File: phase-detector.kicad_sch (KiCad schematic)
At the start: 32 parts, among them J1 Conn_Coaxial_Small, J2 Conn_Coaxial_Small, J3 Conn_Coaxial_Small, J4 Conn_Coaxial_Small, J5 Conn_Coaxial_Small, J6 Conn_Coaxial_Small, J7 Conn_01x14_Socket, U1 ICM-20948, U2 MIC5219-3.3YM5, U3 MIC5219-3.3YM5

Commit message: Rev 1 ready for review
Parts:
- removed U1: ICM-20948, Sensor_Motion:InvenSense_QFN-24_3x3mm_P0.4mm, symbol Sensor_Motion:ICM-20948
- added TP1: INT_2, phase-detector:Test_Via, symbol Connector:TestPoint
- added TP10, TP11, TP12, TP13, TP9: ~{IRQ}, phase-detector:Test_Via, symbol Connector:TestPoint
- added TP2: DRDY, phase-detector:Test_Via, symbol Connector:TestPoint
- added TP3: INT_1, phase-detector:Test_Via, symbol Connector:TestPoint
- added TP4, TP5, TP6, TP7, TP8: Vref, phase-detector:Test_Via, symbol Connector:TestPoint
- added U14: LSM303C, Package_LGA:LGA-12_2x2mm_P0.5mm, symbol Sensor_Motion:LSM303C
- C1: footprint (none) -> Capacitor_SMD:C_0402_1005Metric
- C136, C137, C138, C139: value 10nF -> 100pF
- C2: footprint (none) -> Capacitor_SMD:C_0805_2012Metric
- C5: value 100nF -> 220nF
- R43, R44, R45, R46: value 50 -> 75
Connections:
- net +3.3V-D: now also U14.10 (VDDIO), U14.9 (VDD)
- net AD8302/V_REF: now also TP4.1
- net AD8303/V_REF: now also TP5.1
- net AD8304/V_REF: now also TP6.1
- net AD8305/V_REF: now also TP7.1
- net AD8306/V_REF: now also TP8.1
- net ADC/MDAT: now also TP9.1
- net ADC1/MDAT: now also TP10.1
- net ADC2/MDAT: now also TP11.1
- net ADC3/MDAT: now also TP12.1
- net ADC4/MDAT: now also TP13.1
- net CS0: now also J7.8 (Pin_8); no longer J7.7 (Pin_7)
- net CS1: now also J7.11 (Pin_11); no longer J7.8 (Pin_8)
- net CS2: now also J7.12 (Pin_12); no longer J7.9 (Pin_9)
- net CS3: now also J7.9 (Pin_9); no longer J7.10 (Pin_10)
- net CS4: now also J7.10 (Pin_10); no longer J7.11 (Pin_11)
- net CS5: now also J7.7 (Pin_7), U14.2 (CS_XL); no longer J7.12 (Pin_12)
- net GND: now also C5.2, U14.6 (GND), U14.8 (GND); no longer C5.1, J7.6 (Pin_6)
- net MCLK_EN: now also J7.5 (Pin_5); no longer J7.4 (Pin_4)
- net MISO: now also J7.3 (Pin_3); no longer J7.2 (Pin_2)
- net MOSI: now also J7.4 (Pin_4), U14.4 (SDA/SDI/SDO); no longer J7.3 (Pin_3)
- net SCK: now also J7.2 (Pin_2), U14.1 (SCL/SPC); no longer J7.5 (Pin_5)
- new net: TP3.1, U14.12 (INT_XL)
- new net: TP1.1, U14.11 (DRDY_MAG)
- new net: TP2.1, U14.7 (INT_MAG)
- new net: C5.1, U14.5 (C1)
- new net CS6: J7.6 (Pin_6), U14.3 (CS_MAG)
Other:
- note removed: "TODO: add level shifter"
- moved on the sheet: C1, C2

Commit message: moon
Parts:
- C2: footprint Capacitor_SMD:C_0805_2012Metric -> Capacitor_SMD:C_0603_1608Metric
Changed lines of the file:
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@@
 			)
 		)
-		(property "Footprint" "Capacitor_SMD:C_0805_2012Metric"
+		(property "Footprint" "Capacitor_SMD:C_0603_1608Metric"
 			(at 238.76 74.93 0)
 			(effects

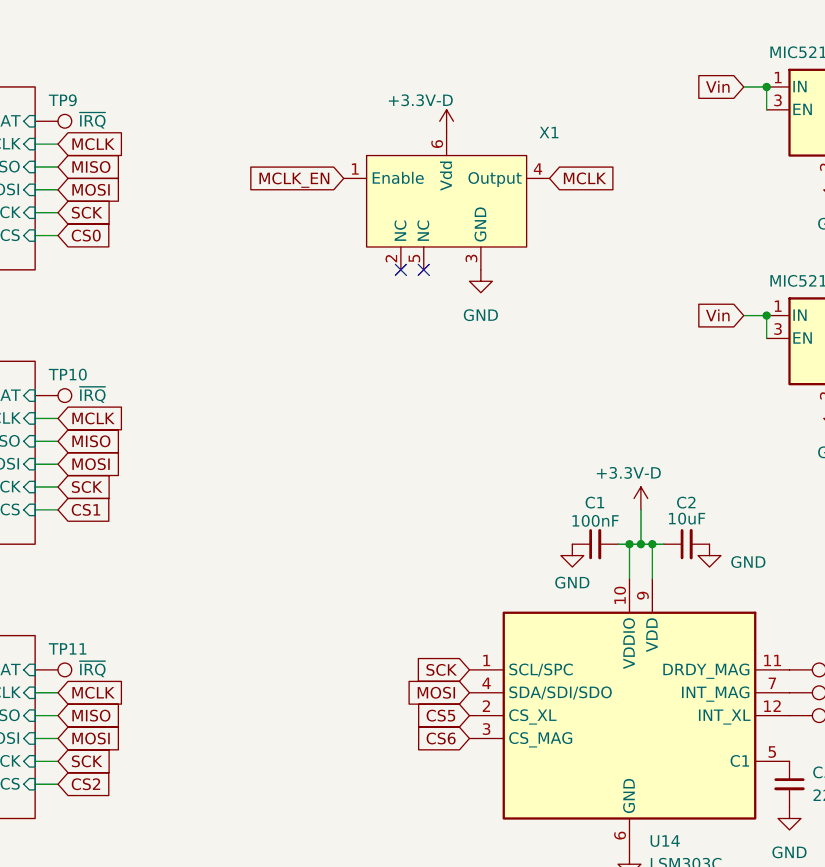
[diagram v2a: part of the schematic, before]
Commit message: load capacitor and shield paste
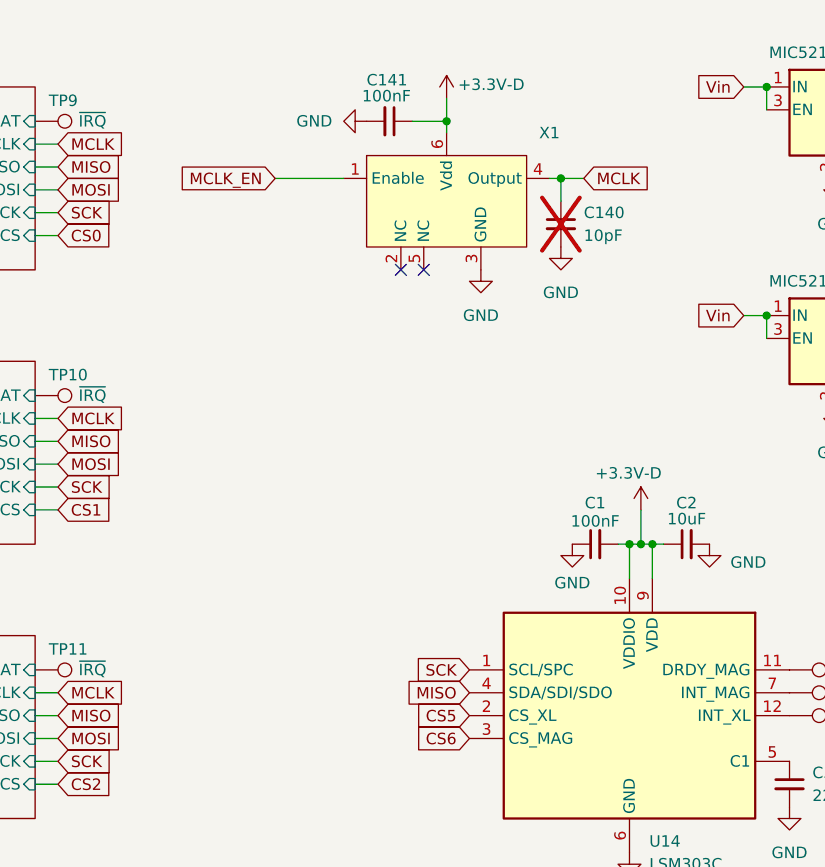
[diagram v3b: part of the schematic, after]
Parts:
- added C140: 10pF, Capacitor_SMD:C_0402_1005Metric, symbol Device:C_Small
- added C141: 100nF, Capacitor_SMD:C_0402_1005Metric, symbol Device:C_Small
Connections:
- net +3.3V-D: now also C141.1
- net GND: now also C140.2, C141.2
- net MCLK: now also C140.1
- net MISO: now also U14.4 (SDA/SDI/SDO)
- net MOSI: no longer U14.4 (SDA/SDI/SDO)

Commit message: boards ordered
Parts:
- added H1, H2, H3, H4, H5: MountingHole_Pad, MountingHole:MountingHole_3.2mm_M3_Pad_TopBottom, symbol Mechanical:MountingHole_Pad
- J1, J2, J3, J4, J5: footprint Connector_Coaxial:SMA_Amphenol_132289_EdgeMount -> phase-detector:SMA_Amphenol_132289_EdgeMount
- J6: footprint Connector_Coaxial:SMA_Amphenol_132291-12_Vertical -> Connector_Coaxial:SMA_Amphenol_132134_Vertical
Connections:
- net GND: now also H1.1, H2.1, H3.1, H4.1, H5.1
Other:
- moved on the sheet: C1, C2, C5, TP1, TP2, TP3, U14
